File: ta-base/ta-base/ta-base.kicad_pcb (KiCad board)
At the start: 2 copper layers, 64 x 58 mm, 0 parts

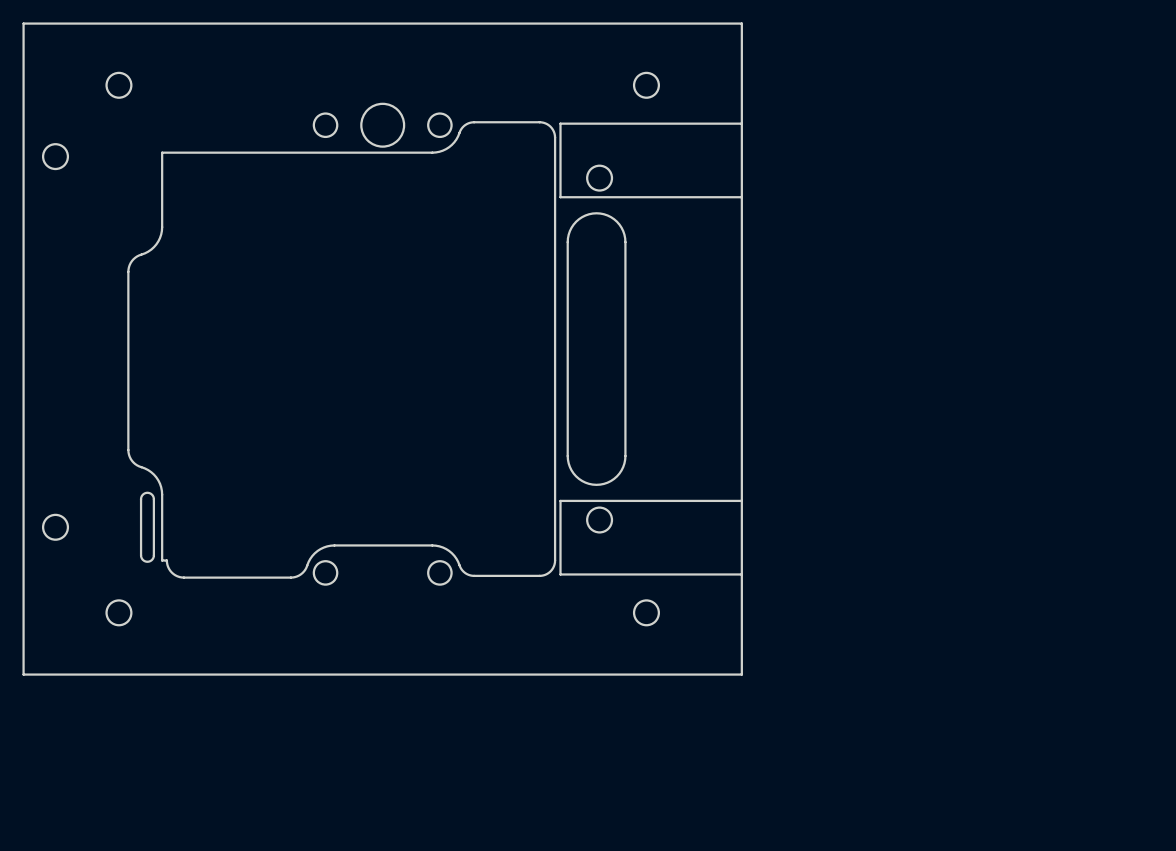
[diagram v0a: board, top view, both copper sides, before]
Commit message: Need to patch symbols and footprints together and route
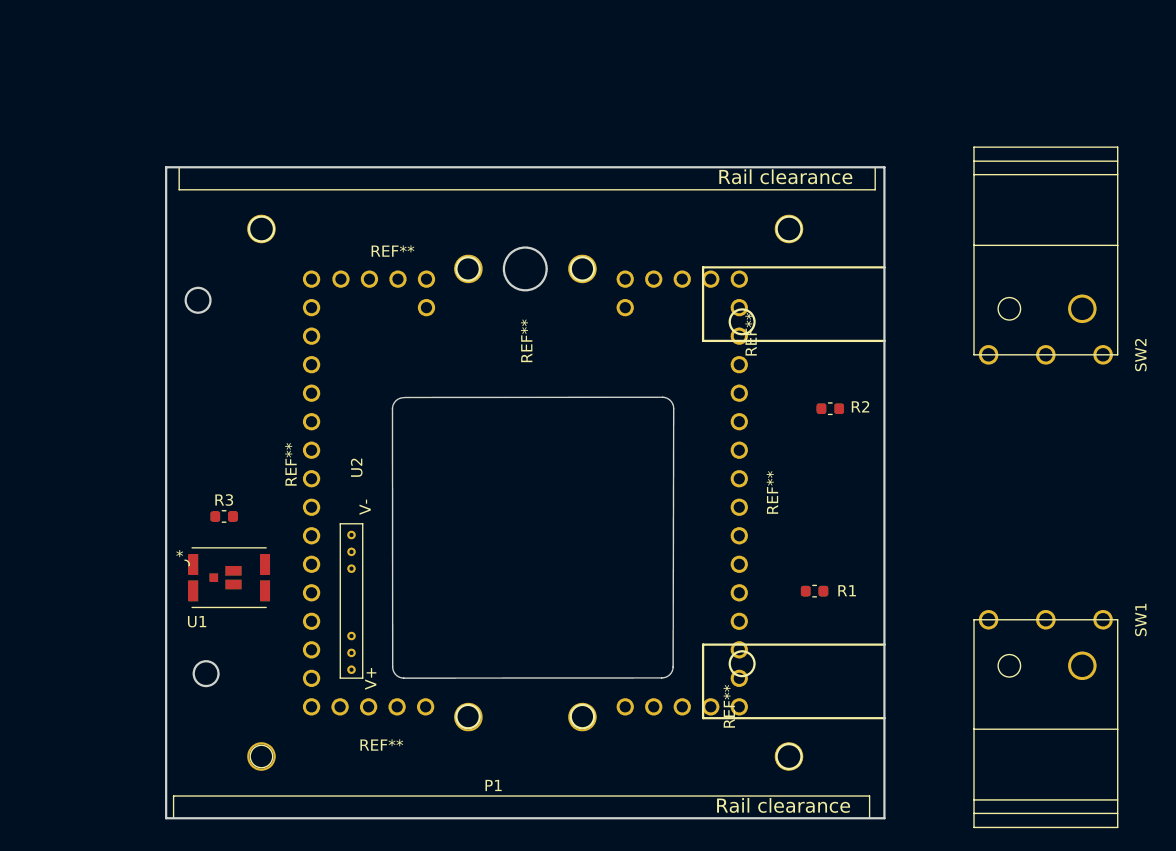
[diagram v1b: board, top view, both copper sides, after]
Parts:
- added P1: Gnd_Screws, ta-base:chassis_gnd_screws, F.Cu at (146.3, 128.0)
- added R1: 100, ta-base:R_0603_1608Metric_base_cpy, F.Cu at (195.6, 113.2)
- added R2: 100, ta-base:R_0603_1608Metric_base_cpy, F.Cu at (197.0, 97.0)
- added R3: 1.5M, ta-base:R_0603_1608Metric_base_cpy, F.Cu at (143.0, 106.6)
- added REF**: PinSocket_1x5_right_TartanArtibeus, ta-base:PinSocket_1x5_right_TartanArtibeus_base_cpy, F.Cu at (183.9, 85.5)
- added REF**: PinSocket_1x5_left_TartanArtibeus, ta-base:PinSocket_1x5_left_TartanArtibeus_base_cpy, F.Cu at (155.9, 85.5)
- added REF**: PinSocket_1x4_TartanArtibeus, ta-base:PinSocket_1x4_TartanArtibeus_base_cpy, F.Cu at (182.5, 123.6)
- added REF**: PinSocket_1x4_TartanArtibeus, ta-base:PinSocket_1x4_TartanArtibeus_base_cpy, F.Cu at (157.1, 123.6)
- added REF**: PinSocket_1x16_TartanArtibeus, ta-base:PinSocket_1x16_TartanArtibeus_base_cpy, F.Cu at (188.9, 104.5)
- added REF**: PinSocket_1x16_TartanArtibeus, ta-base:PinSocket_1x16_TartanArtibeus_base_cpy, F.Cu at (150.8, 104.5)
- added REF**: MountingHoles_TartanArtibeus, ta-base:MountingHoles_TartanArtibeus_base_cpy, F.Cu at (169.8, 84.5)
- added SW1: SW_SPDT, ta-base:switch_left, F.Cu at (216.2, 115.8)
- added SW2: SW_SPDT, ta-base:switch_right, F.Cu at (216.2, 92.2)
- added U1: BSB008NE2LXXUMA1, ta-base:BSB008NE2LXXUMA1, F.Cu at (143.4, 112.0)
- added U2: burn_wire, ta-base:burn_wire, F.Cu at (154.3, 111.2)
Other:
- outline, holes or cut-outs redrawn
- net class Default: clearance 0.2 -> 0.1524; trace_width 0.25 -> 0.127; via_dia 0.8 -> 0.635; via_drill 0.4 -> 0.381
- rule pad_to_mask_clearance: 0 -> 0.0127
- rule trace_clearance: 0.2 -> 0.1524
- rule trace_min: 0.2 -> 0.127
- rule via_min_drill: 0.3 -> 0.254
- rule via_min_size: 0.4 -> 0.635
- board text added: "Rail clearance"

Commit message: finalized place and route
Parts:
- removed the REF** at (183.9, 85.5)
- removed the REF** at (155.9, 85.5)
- removed the REF** at (182.5, 123.6)
- removed the REF** at (157.1, 123.6)
- removed the REF** at (188.9, 104.5)
- removed the REF** at (150.8, 104.5)
- removed the REF** at (169.8, 84.5)
- added J1: PinSocket_16_base, ta-base:PinSocket_1x16_TartanArtibeus_base_cpy, F.Cu at (147.0, 104.5)
- added J2: PinSocket_4_base, ta-base:PinSocket_1x4_TartanArtibeus_base_cpy, F.Cu at (178.7, 123.6)
- added J3: PinSocket_4_base, ta-base:PinSocket_1x4_TartanArtibeus_base_cpy, F.Cu at (153.3, 85.5)
- added J4: PinSocket_4_base, ta-base:PinSocket_1x4_TartanArtibeus_base_cpy, F.Cu at (153.3, 123.6)
- added J5: PinSocket_5_base, ta-base:PinSocket_1x5_right_TartanArtibeus_base_cpy, F.Cu at (180.1, 85.5)
- added J6: PinSocket_16_base, ta-base:PinSocket_1x16_TartanArtibeus_base_cpy, F.Cu at (185.1, 104.5)
- added J7: PinSocket_5_base, ta-base:solar_internal, F.Cu at (153.8, 89.6)
- added J8: PinSocket_5_base, ta-base:solar_internal, F.Cu at (193.8, 102.6)
- added P2: Gnd_standoffs, ta-base:MountingHoles_TartanArtibeus_base_cpy, F.Cu at (166.0, 84.5)
- added REF**: MountingHole_6.4mm_M6, MountingHole:MountingHole_6.4mm_M6, F.Cu at (166.0, 90.3)
- U1: value BSB008NE2LXXUMA1 -> TRANS_BSB008NE2LXXUMA1_INF
- moved SW2 23.8 mm to (192.4, 93.4)
- moved SW1 23.8 mm to (192.4, 115.6)
- moved U1 14.0 mm to (152.1, 101.0), turned to 90 degrees
- moved R3 10.8 mm to (153.8, 107.6), turned to 270 degrees
- moved P1 3.80 mm to (142.5, 128.0)
- moved U2 3.80 mm to (150.6, 111.2)
- moved R1 2.90 mm to (197.3, 110.9)
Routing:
- net /V_solar: track 0.00 -> 89.0 mm
- net /Vcap: track 0.00 -> 86.0 mm
- net /BURN_SIG: track 0.00 -> 24.7 mm
- net Net-(U1-Pad4): track 0.00 -> 20.8 mm
- net GND: track 0.00 -> 8.37 mm, vias 0 -> 5
- net Net-(R1-Pad2): track 0.00 -> 6.40 mm
- net Net-(R2-Pad2): track 0.00 -> 5.30 mm
- added copper zone on B.Cu, net GND
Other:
- outline, holes or cut-outs redrawn
- board text added: "GND"
- board text added: "Vcap"
- board text added: "Vsolar"
- board text added: "burn"
- board text added: "ck-ex"
- board text added: "cts-co"
- board text added: "cts-ex"
- board text added: "cts0-co"
- board text added: "dbg0-ct"
- board text added: "dbg1-ct"
- board text added: "dbg2-ct"
- board text added: "pclk-co"
- board text added: "pdio-co"
- board text added: "rst-ct"
- board text added: "rst-ex"
- board text added: "rts-co"
- board text added: "rts-ex"
- board text added: "rts0-co"
- board text added: "rx-co"
- board text added: "rx-ex"
- board text added: "rx0-co"
- board text added: "scl"
- board text added: "sda"
- board text added: "swclk-ex"
- board text added: "swdio-ex"
- board text added: "tst-ct"
- board text added: "tx-co"
- board text added: "tx-ex"
- board text added: "tx0-co"
- board text added: "vdd-co"
- board text added: "vdd-ct"
- board text added: "vdd-ex"
- board text added: "vdd-gps"

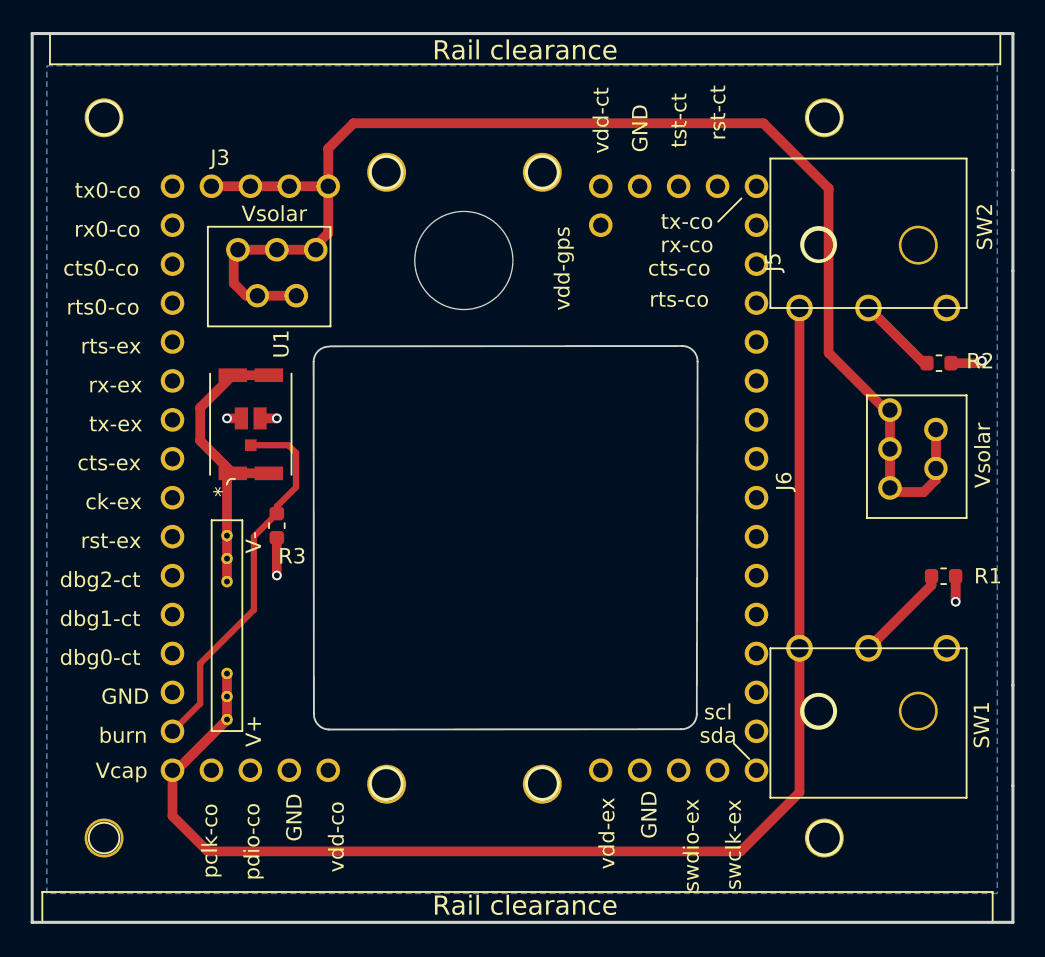
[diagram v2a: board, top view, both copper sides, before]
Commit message: updated line width on edge cuts for base plate
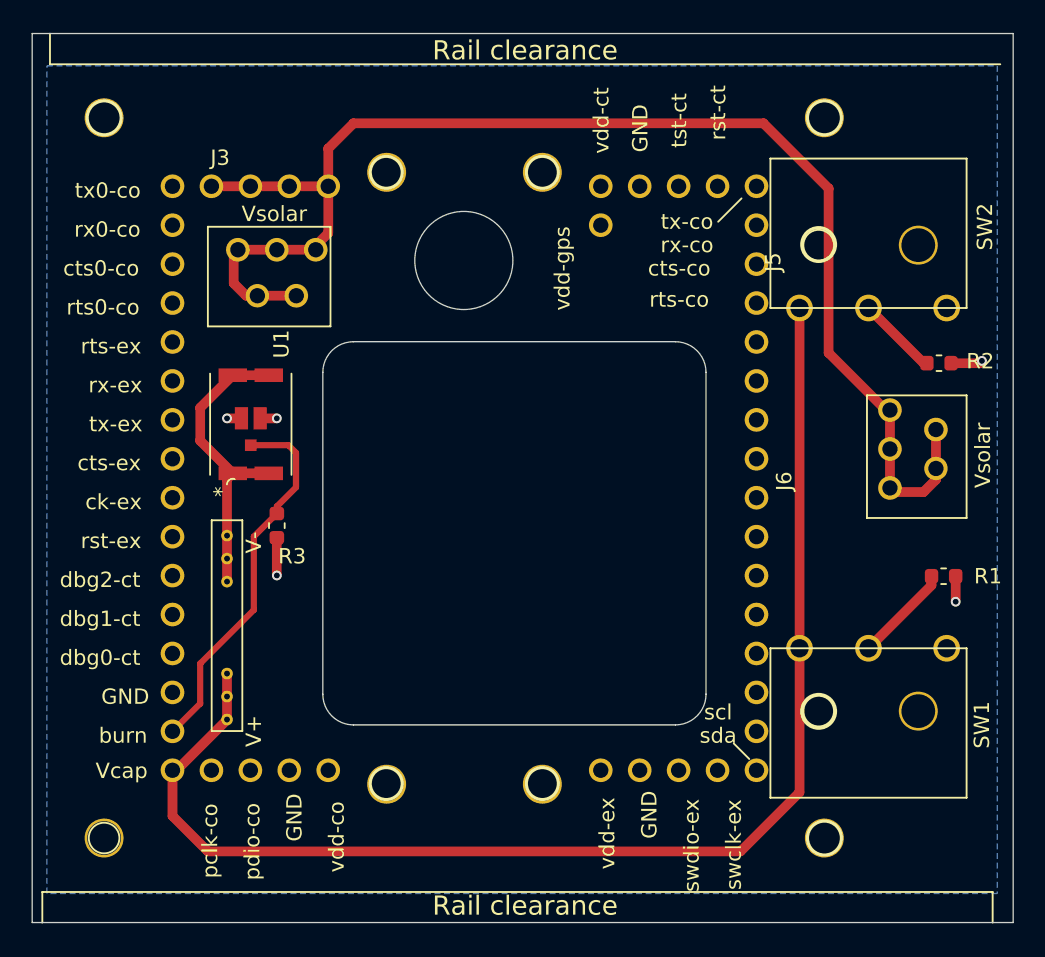
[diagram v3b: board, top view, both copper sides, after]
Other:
- outline, holes or cut-outs redrawn

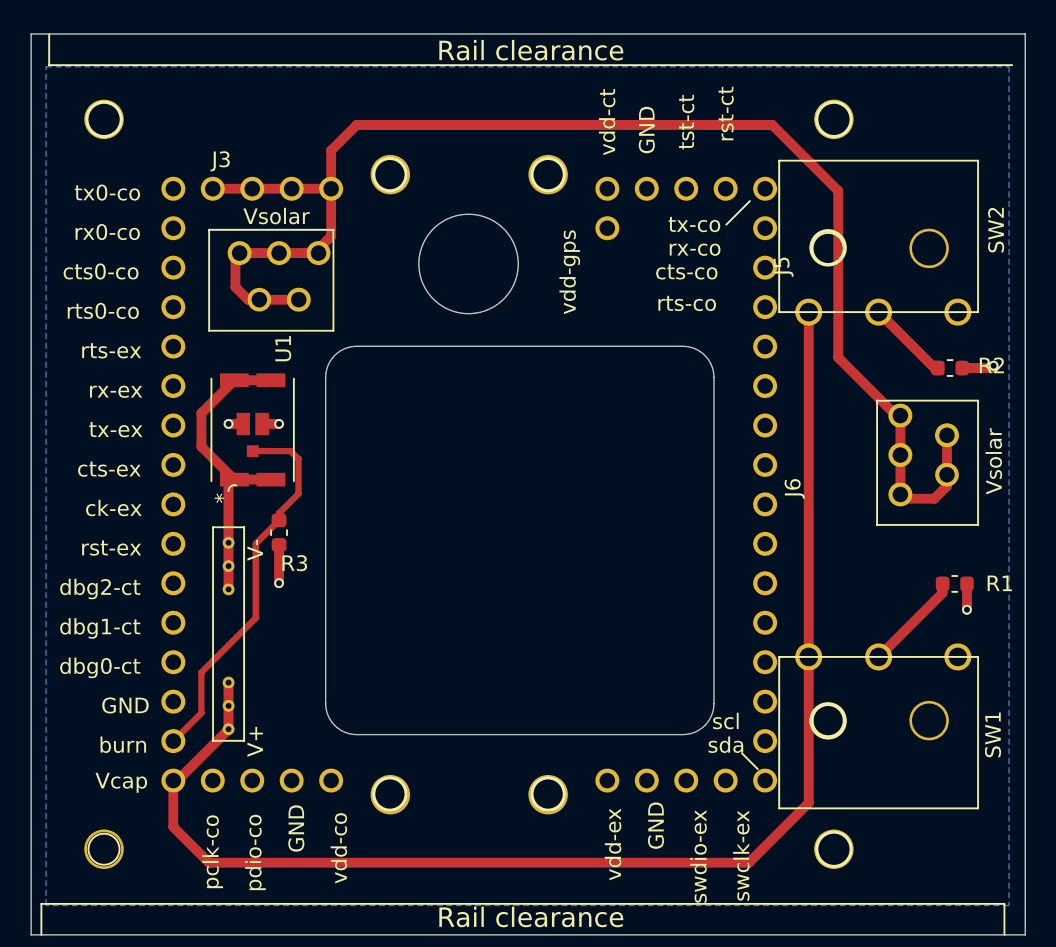
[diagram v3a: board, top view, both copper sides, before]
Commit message: added new solar header
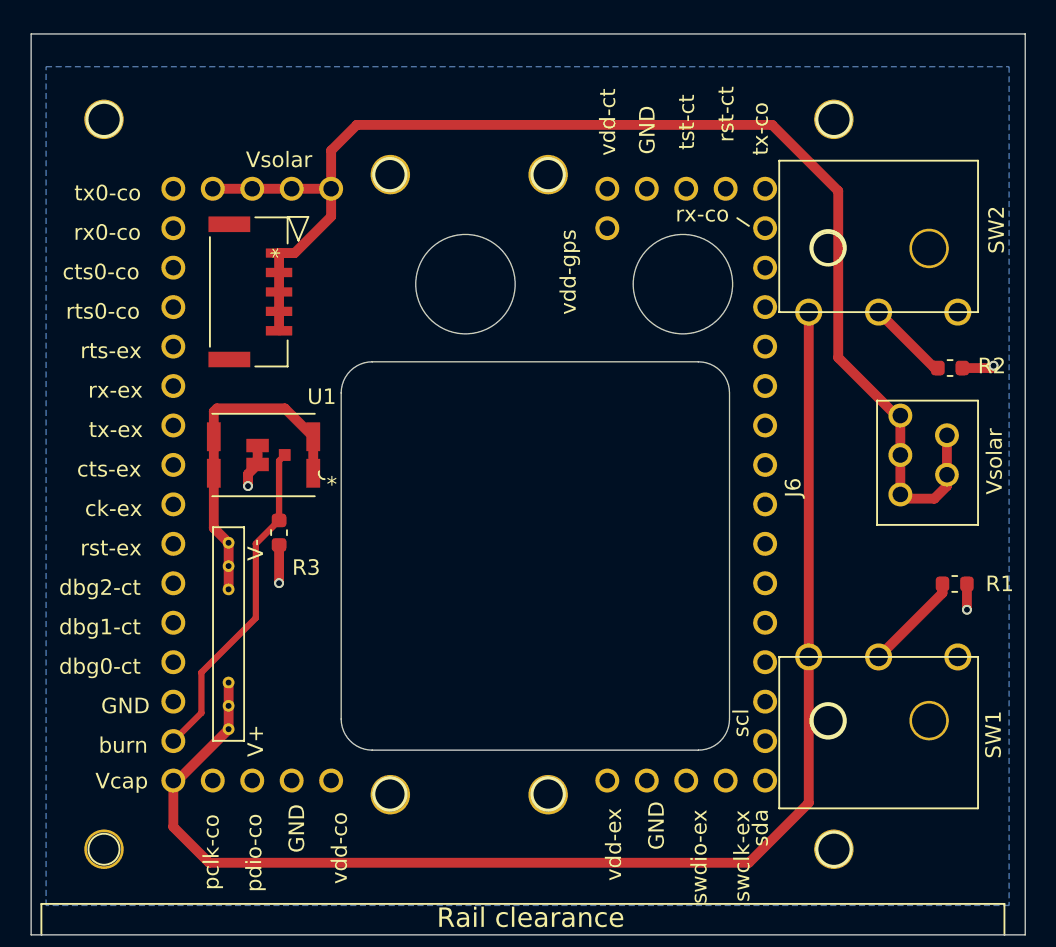
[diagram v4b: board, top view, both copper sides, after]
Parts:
- added REF**: MountingHole_6.4mm_M6, MountingHole:MountingHole_6.4mm_M6, F.Cu at (165.8, 91.6)
- J7: footprint ta-base:solar_internal -> ta-base:5023860570
- U1: value TRANS_BSB008NE2LXXUMA1_INF -> BSB008NE2LXXUMA1
- moved REF** 13.9 mm to (179.8, 91.6)
- moved U1 1.76 mm to (152.8, 102.6), turned to 180 degrees
- turned J7 to 90 degrees
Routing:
- net /V_solar: track 89.0 -> 84.1 mm
- net /BURN_SIG: track 24.7 -> 21.4 mm
- net GND: track 8.37 -> 9.20 mm, vias 5 -> 4
- net Net-(U1-Pad4): track 20.8 -> 21.4 mm
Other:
- outline, holes or cut-outs redrawn
- board text removed: "cts-co"
- board text removed: "rts-co"

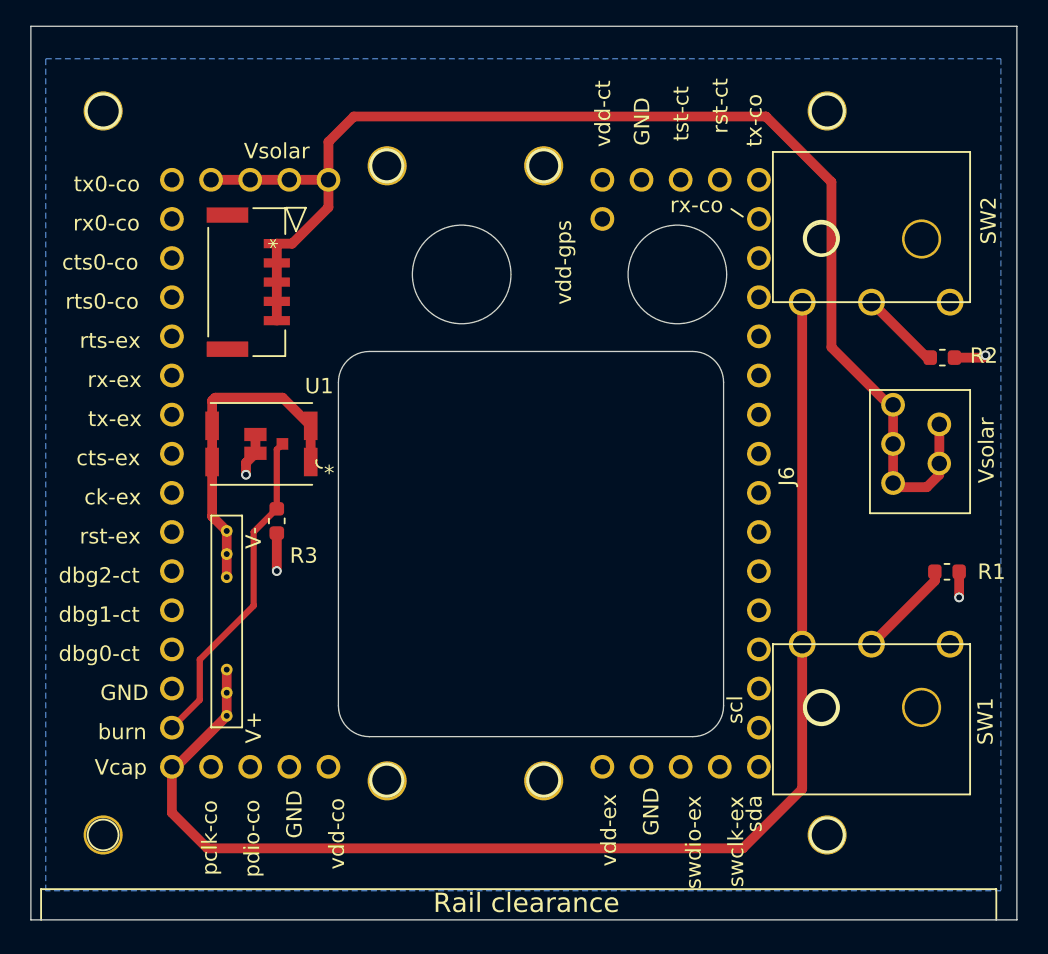
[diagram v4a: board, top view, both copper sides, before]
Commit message: added connector on outside
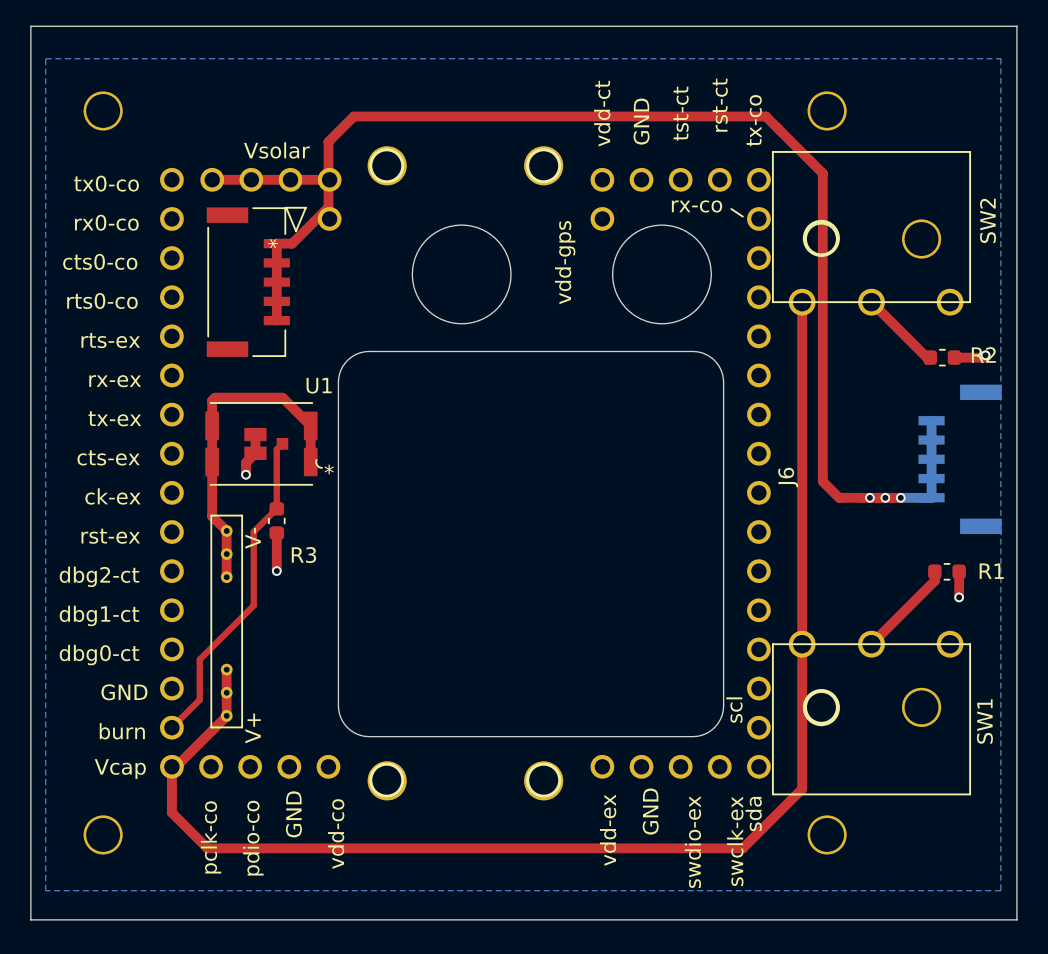
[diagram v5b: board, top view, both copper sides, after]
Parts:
- J3: value PinSocket_4_base -> PinSocket_5_base; footprint ta-base:PinSocket_1x4_TartanArtibeus_base_cpy -> ta-base:5023860570; moved to B.Cu
- J8: footprint ta-base:solar_internal -> ta-base:PinSocket_1x5_left_TartanArtibeus_base_cpy
- moved J3 45.7 mm to (196.3, 101.1), turned to 90 degrees
- moved J8 45.1 mm to (152.1, 85.5), turned to 90 degrees
- moved REF** 1.00 mm to (178.8, 91.6)
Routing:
- net /V_solar: track 84.1 -> 90.0 mm, vias 0 -> 3
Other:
- board text removed: "Rail clearance"
